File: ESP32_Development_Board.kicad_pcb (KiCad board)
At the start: 2 copper layers, 47 parts, among them J1 Conn_01x17_Pin, J2 Conn_01x17_Pin, J3 Conn_01x03_Pin, J4 USB_B_Micro, J5 Conn_01x02_Pin, Q1 NPN, Q2 NPN, Q3 Q_NMOS_GDS, Q4 Q_NMOS_GDS, SW1 SW_Push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

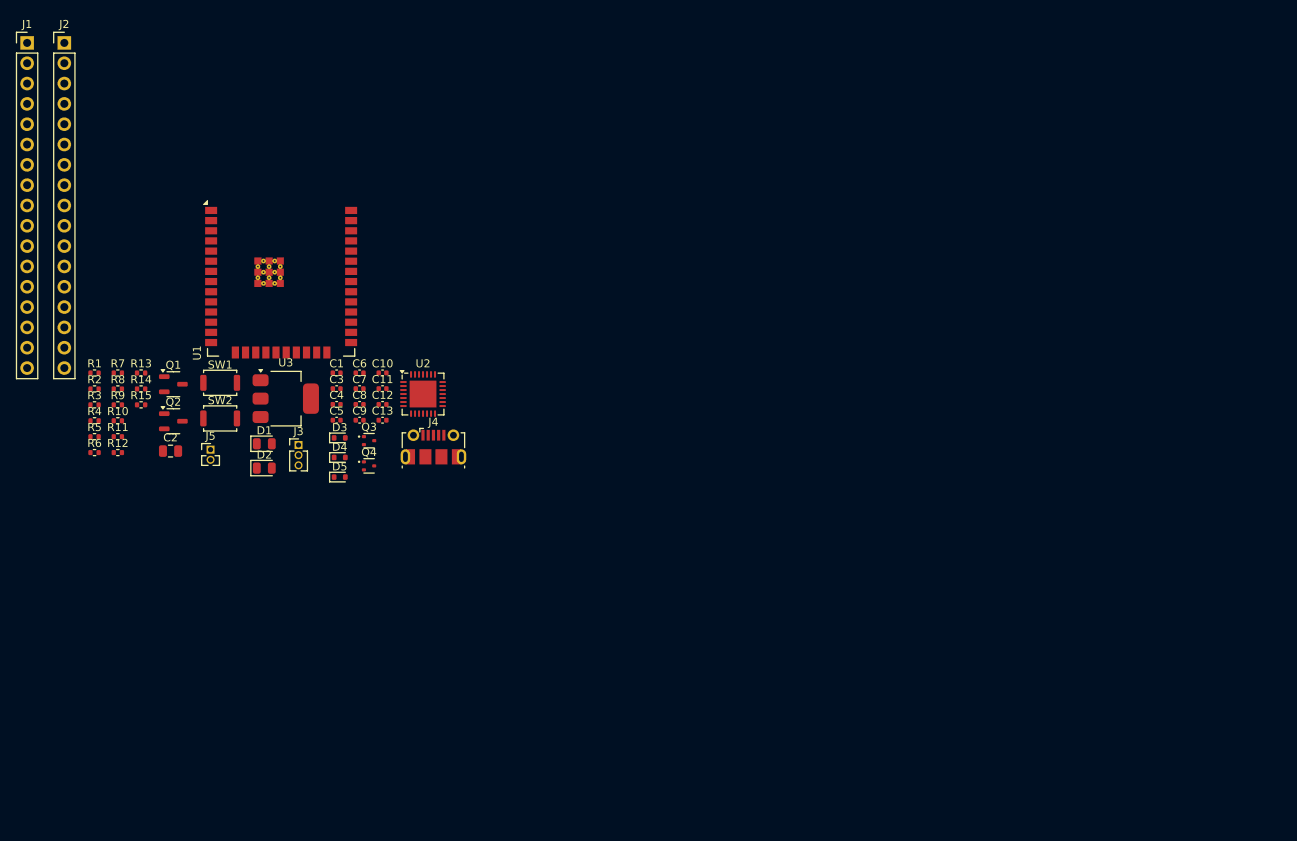
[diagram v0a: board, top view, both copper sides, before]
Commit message: Placed Components
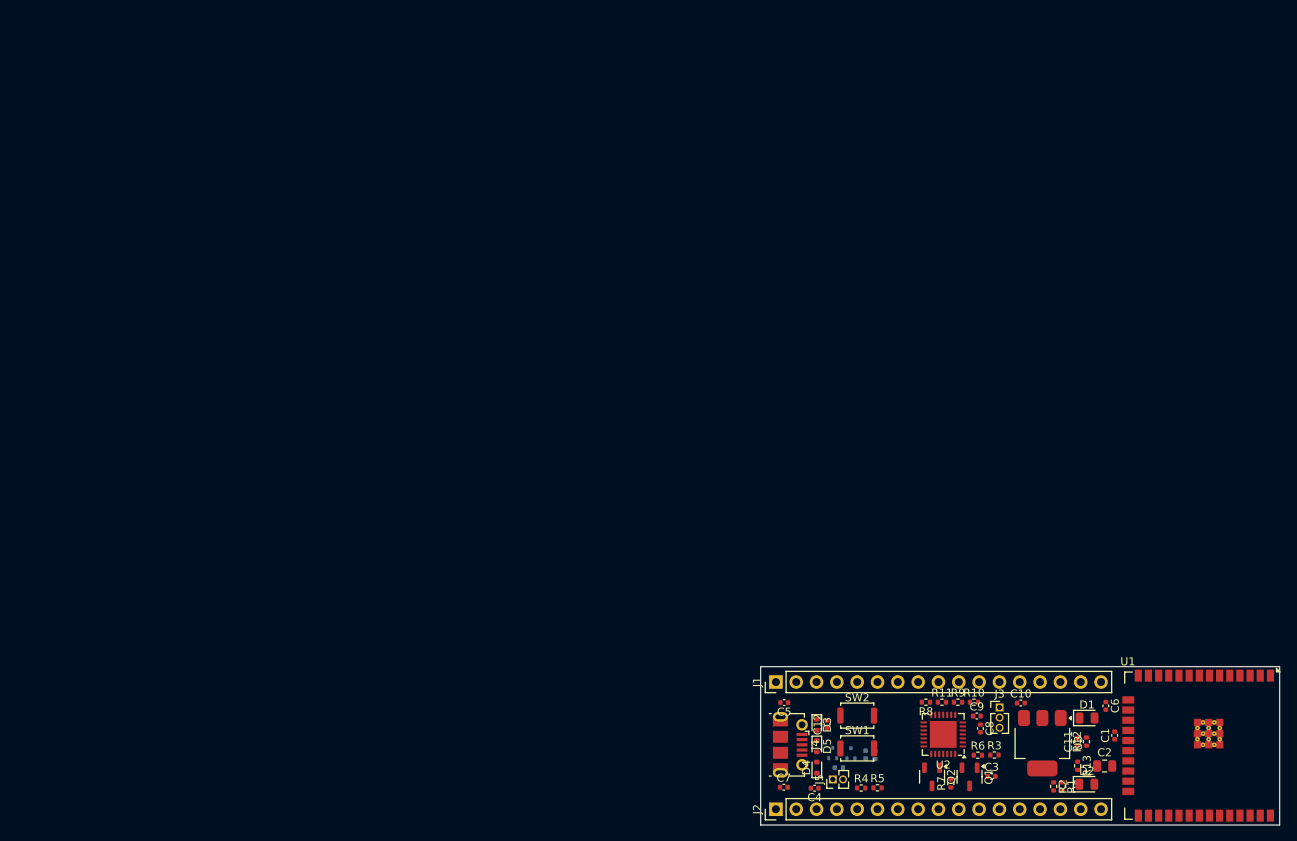
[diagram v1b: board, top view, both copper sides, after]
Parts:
- C13, Q3, Q4, R14, R15: moved to B.Cu
- moved U1 133.5 mm to (191.4, 102.6), turned to -90 degrees
- moved R1 131.5 mm to (170.6, 107.7), turned to -90 degrees
- moved J2 130.7 mm to (134.8, 110.5), turned to 90 degrees
- moved R2 129.8 mm to (169.5, 107.7), turned to -90 degrees
- moved R13 126.9 mm to (172.5, 105.1), turned to -90 degrees
- moved R12 126.4 mm to (173.6, 102.1), turned to 90 degrees
- moved C2 123.2 mm to (175.9, 105.2)
- moved J1 123.1 mm to (134.8, 94.7), turned to 90 degrees
- moved R3 120.7 mm to (162.1, 103.8)
- moved R6 116.7 mm to (160.1, 103.8)
- moved R7 116.1 mm to (156.7, 107.3), turned to 90 degrees
- moved R10 112.6 mm to (159.6, 97.2)
- moved R9 111.4 mm to (157.6, 97.2)
- moved Q1 111.0 mm to (159.0, 106.5), turned to -90 degrees
- moved D2 110.1 mm to (173.7, 107.4)
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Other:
- board outline added: 64.9 x 19.8 mm

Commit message: Aug 16, 2025
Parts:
- J5: moved to B.Cu
- U3: footprint Package_TO_SOT_SMD:SOT-223-3_TabPin2 -> Package_TO_SOT_SMD:SOT-89-3
- moved R1 97.4 mm to (76.0, 84.4), turned to 0 degrees
- moved R2 95.9 mm to (76.0, 86.4), turned to 0 degrees
- moved R13 93.1 mm to (81.8, 84.4), turned to 0 degrees
- moved C2 91.1 mm to (85.5, 94.2)
- moved C1 87.8 mm to (90.3, 88.6), turned to 0 degrees
- moved D2 85.7 mm to (91.1, 84.5)
- moved R6 84.6 mm to (76.0, 94.4)
- moved R7 81.1 mm to (78.9, 84.4), turned to 0 degrees
- moved R10 81.0 mm to (78.9, 90.4)
- moved R9 79.2 mm to (78.9, 88.4)
- moved R11 76.8 mm to (78.9, 92.4)
- moved Q1 76.0 mm to (85.8, 85.8), turned to 0 degrees
- moved R8 75.4 mm to (78.9, 86.4), turned to 0 degrees
- moved R5 73.2 mm to (76.0, 92.4)
- moved R4 71.7 mm to (76.0, 90.4)
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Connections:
- D4 pad 2: /USB_DN -> /USB_DP
- D5 pad 2: /USB_DP -> /USB_DN
- J4 pad 2: /USB_DP -> /USB_DN
- J4 pad 3: /USB_DN -> /USB_DP
- Q3 pad 2: /USB_DN -> /USB_DP
- Q4 pad 2: /USB_DP -> /USB_DN
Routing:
- net GND: track 0.00 -> 25.7 mm, vias 0 -> 14
- net +3.3V: track 0.00 -> 22.4 mm, vias 0 -> 4
- net Net-(J5-Pin_2): track 0.00 -> 10.9 mm
- net +5VD: track 0.00 -> 6.58 mm
- net /EN: track 0.00 -> 5.38 mm
- net /USB_DN: track 0.00 -> 5.13 mm, vias 0 -> 1
- net /USB_DP: track 0.00 -> 5.12 mm, vias 0 -> 1
- net +5VA: track 0.00 -> 4.89 mm
- net +5V: track 0.00 -> 4.10 mm
- net /IO23: track 0.00 -> 3.79 mm
- net Net-(D1-A): track 0.00 -> 1.68 mm
- added copper zone on In1.Cu, net +3.3V
- added copper zone on In2.Cu, net GND
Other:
- board size 64.9 x 19.8 mm -> 70 x 20.3 mm
- copper layers 2 -> 4

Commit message: Commit at 2025-08-18 15:00:00
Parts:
- moved R2 83.6 mm to (157.6, 104.8), turned to -90 degrees
- moved R1 74.9 mm to (148.8, 101.8), turned to 180 degrees
- moved C2 70.9 mm to (156.3, 91.8), turned to 90 degrees
- moved C1 67.1 mm to (157.1, 94.7), turned to -90 degrees
- moved R5 63.1 mm to (138.5, 100.6), turned to 90 degrees
- moved R4 62.3 mm to (137.4, 100.6), turned to 90 degrees
- moved R9 61.5 mm to (140.2, 92.3), turned to -90 degrees
- moved R10 60.3 mm to (139.2, 92.3), turned to 90 degrees
- moved R11 59.2 mm to (138.1, 92.3), turned to -90 degrees
- moved R8 58.4 mm to (137.0, 92.3), turned to 90 degrees
- moved C8 49.0 mm to (142.1, 94.6), turned to 90 degrees
- moved C9 47.9 mm to (141.0, 94.6), turned to 90 degrees
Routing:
- net GND: track 25.7 -> 31.3 mm, vias 14 -> 16
- net Net-(U1-IO0): track 0.00 -> 3.27 mm
- net +3.3V: track 22.4 -> 25.5 mm, vias 4 -> 5
- net /IO0_CON: track 0.00 -> 2.43 mm

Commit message: Commit at 2025-08-18 17:00:00
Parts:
- moved R6 66.4 mm to (142.1, 100.6), turned to -90 degrees
- moved R7 60.6 mm to (137.1, 101.1), turned to -90 degrees
- moved Q2 60.1 mm to (145.1, 100.5), turned to 180 degrees
- moved R13 53.5 mm to (133.9, 96.2), turned to 90 degrees
- moved Q1 50.8 mm to (134.5, 100.5)
- moved D2 46.1 mm to (135.5, 96.9), turned to 90 degrees
- moved C4 34.6 mm to (124.7, 95.5)
- moved U2 2.48 mm to (139.8, 96.5)
- moved C8 2.47 mm to (144.6, 94.6)
- moved C9 2.47 mm to (143.5, 94.6)
- moved R10 2.47 mm to (141.7, 92.3)
- moved R11 2.47 mm to (140.6, 92.3)
- moved R4 2.47 mm to (139.9, 100.6)
- moved R5 2.47 mm to (141.0, 100.6)
- moved R8 2.47 mm to (139.5, 92.3)
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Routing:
- net GND: track 31.3 -> 37.7 mm, vias 16 -> 20
- net +3.3V: track 25.5 -> 31.4 mm, vias 5 -> 7
- net /DTR: track 0.00 -> 3.59 mm
- net /USB_DN: track 5.13 -> 8.14 mm, vias 1 -> 2
- net /USB_DP: track 5.12 -> 8.13 mm, vias 1 -> 2
- net Net-(U2-VBUS): track 0.00 -> 2.42 mm
- net /TXD: track 0.00 -> 1.44 mm
- net Net-(U2-~{SUSPEND}): track 0.00 -> 1.34 mm
- net Net-(U2-~{RST}): track 0.00 -> 1.32 mm
- net /RXD: track 0.00 -> 1.22 mm
- net +5VA: track 4.89 -> 5.88 mm, vias 0 -> 1

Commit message: Commit at 2025-08-18 18:00:00
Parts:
- moved R7 1.77 mm to (138.8, 100.6)
- moved R15 1.40 mm to (118.3, 101.8)
- moved R14 1.01 mm to (118.3, 99.7), turned to 180 degrees
- moved C13 0.98 mm to (118.3, 100.7), turned to 180 degrees
- moved Q3 0.92 mm to (118.5, 97.9)
- moved Q4 0.89 mm to (118.3, 93.8)
- moved C6 0.41 mm to (155.8, 87.8)
- moved C8 0.36 mm to (144.6, 94.3)
- moved C9 0.36 mm to (143.5, 94.3)
- moved Q1 0.09 mm to (134.5, 100.5)
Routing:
- net /USB_DP: track 8.13 -> 33.8 mm
- net /USB_DN: track 8.14 -> 33.8 mm
- net Net-(J5-Pin_2): track 10.9 -> 0.01 mm
- net GND: track 37.7 -> 27.6 mm, vias 20 -> 17
- net +3.3V: track 31.4 -> 24.9 mm, vias 7 -> 9
- net /RTS: track 0.00 -> 4.72 mm
- net Net-(D2-A): track 0.00 -> 1.70 mm
- net /IO23: track 3.79 -> 2.39 mm

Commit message: Commit at 2025-08-18 20:04:58
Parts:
- moved J5 1.43 mm to (120.9, 99.8)
- moved Q3 0.58 mm to (118.5, 97.4)
- moved Q4 0.47 mm to (118.4, 94.3)
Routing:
- net Net-(J5-Pin_2): track 0.01 -> 19.4 mm
- net GND: track 27.6 -> 32.3 mm, vias 17 -> 19
- net /USB_DP: track 33.8 -> 35.0 mm
- net /USB_DN: track 33.8 -> 35.0 mm
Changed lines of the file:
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@@
 	(footprint "Connector_PinHeader_1.27mm:PinHeader_1x02_P1.27mm_Vertical"
 		(layer "B.Cu")
-		(at 121.825 98.7 180)
+		(at 120.94 99.82 180)
 		(descr "Through hole straight pin header, 1x02, 1.27mm pitch, single row")
 		(tags "Through hole pin header THT 1x02 1.27mm single row")
@@
 	(footprint "Package_TO_SOT_SMD:SOT-523"
 		(layer "B.Cu")
-		(at 118.45 97.94)
+		(at 118.455 97.36)
 		(descr "SOT523, https://www.diodes.com/assets/Package-Files/SOT523.pdf")
 		(tags "SOT-523")
@@
 	(footprint "Package_TO_SOT_SMD:SOT-523"
 		(layer "B.Cu")
-		(at 118.35 93.8175 90)
+		(at 118.36 94.29 90)
 		(descr "SOT523, https://www.diodes.com/assets/Package-Files/SOT523.pdf")
 		(tags "SOT-523")
@@
 	)
 	(via
+		(at 116.9 99.66)
+		(size 0.6)
+		(drill 0.3)
+		(layers "F.Cu" "B.Cu")
+		(net 1)
+	)
+	(via
 		(at 156.65 87.37)
 		(size 0.6)
@@
 	)
 	(via
+		(at 118.83 98.35)
+		(size 0.6)
+		(drill 0.3)
+		(layers "F.Cu" "B.Cu")
+		(net 1)
+	)
+	(via
 		(at 116.225 90.825)
 		(size 0.6)
 		(drill 0.3)
 		(layers "F.Cu" "B.Cu")
+		(net 1)
+	)
+	(segment
+		(start 117.81 100.67)
+		(end 117.87 100.73)
+		(width 0.5334)
+		(layer "B.Cu")
+		(net 1)
+	)
+	(segment
+		(start 116.9 93.95)
+		(end 117.205 93.645)
+		(width 0.5334)
+		(layer "B.Cu")
+		(net 1)
+	)
+	(segment
+		(start 117.205 93.645)
+		(end 118.36 93.645)
+		(width 0.5334)
+		(layer "B.Cu")
+		(net 1)
+	)
+	(segment
+		(start 119.1 97.36)
+		(end 119.1 98.08)
+		(width 0.5334)
+		(layer "B.Cu")
+		(net 1)
+	)
+	(segment
+		(start 117.81 99.66)
+		(end 117.81 100.67)
+		(width 0.5334)
+		(layer "B.Cu")
+		(net 1)
+	)
+	(segment
+		(start 119.1 98.08)
+		(end 118.83 98.35)
+		(width 0.5334)
+		(layer "B.Cu")
+		(net 1)
+	)
+	(segment
+		(start 117.81 99.66)
+		(end 116.9 99.66)
+		(width 0.5334)
+		(layer "B.Cu")
 		(net 1)
 	)
@@
 	)
 	(segment
-		(start 118.83 101.8)
+		(start 118.83 99.66)
+		(end 118.83 99.3)
+		(width 0.2)
+		(layer "B.Cu")
+		(net 8)
+	)
+	(segment
+		(start 116.3 98.32)
+		(end 116.69 98.71)
+		(width 0.2)
+		(layer "B.Cu")
+		(net 8)
+	)
+	(segment
+		(start 117.81 98.28)
+		(end 117.81 97.86)
+		(width 0.2)
+		(layer "B.Cu")
+		(net 8)
+	)
+	(segment
+		(start 116.7 92.72)
+		(end 116.3 93.12)
+		(width 0.2)
+		(layer "B.Cu")
+		(net 8)
+	)
+	(segment
+		(start 116.69 98.71)
+		(end 117.38 98.71)
+		(width 0.2)
+		(layer "B.Cu")
+		(net 8)
+	)
+	(segment
+		(start 119.18 92.72)
+		(end 116.7 92.72)
+		(width 0.2)
+		(layer "B.Cu")
+		(net 8)
+	)
+	(segment
+		(start 116.3 93.12)
+		(end 116.3 98.32)
+		(width 0.2)
+		(layer "B.Cu")
+		(net 8)
+	)
+	(segment
+		(start 120.54 101.09)
+		(end 119.82 101.81)
+		(width 0.2)
+		(layer "B.Cu")
+		(net 8)
+	)
+	(segment
+		(start 119.82 101.81)
 		(end 118.83 101.81)
+		(width 0.2)
+		(layer "B.Cu")
+		(net 8)
+	)
+	(segment
+		(start 118.86 94.935)
+		(end 118.86 94.42)
+		(width 0.2)
+		(layer "B.Cu")
+		(net 8)
+	)
+	(segment
+		(start 117.38 98.71)
+		(end 117.81 98.28)
+		(width 0.2)
+		(layer "B.Cu")
+		(net 8)
+	)
+	(segment
+		(start 119.4 93.88)
+		(end 119.4 92.94)
+		(width 0.2)
+		(layer "B.Cu")
+		(net 8)
+	)
+	(segment
+		(start 119.4 92.94)
+		(end 119.18 92.72)
+		(width 0.2)
+		(layer "B.Cu")
+		(net 8)
+	)
+	(segment
+		(start 118.83 99.66)
+		(end 118.83 101.81)
+		(width 0.2)
+		(layer "B.Cu")
+		(net 8)
+	)
+	(segment
+		(start 120.94 101.09)
+		(end 120.54 101.09)
+		(width 0.2)
+		(layer "B.Cu")
+		(net 8)
+	)
+	(segment
+		(start 118.83 99.3)
+		(end 117.81 98.28)
+		(width 0.2)
+		(layer "B.Cu")
+		(net 8)
+	)
+	(segment
+		(start 118.86 94.42)
+		(end 119.4 93.88)
 		(width 0.2)
 		(layer "B.Cu")
@@
 	)
 	(segment
+		(start 117.315 94.935)
+		(end 116.9 95.35)
+		(width 0.2)
+		(layer "B.Cu")
+		(net 12)
+	)
+	(segment
 		(start 119.469301 95.712499)
 		(end 120.0468 95.135)
@@
 	)
 	(segment
+		(start 117.86 94.935)
+		(end 117.315 94.935)
+		(width 0.2)
+		(layer "B.Cu")
+		(net 12)
+	)
+	(segment
 		(start 143.530001 96.400001)
 		(end 143.8925 96.7625)
@@
 	)
 	(segment
+		(start 117.81 96.86)
+		(end 117.09 96.86)
+		(width 0.2)
+		(layer "B.Cu")
+		(net 13)
+	)
+	(segment
+		(start 117.09 96.86)
+		(end 116.9 96.67)
+		(width 0.2)
+		(layer "B.Cu")
+		(net 13)
+	)
+	(segment
 		(start 116.9 96.525)
 		(end 117.262499 96.162501)
@@
 		(width 0.2)
 		(layer "B.Cu")
+		(net 13)
+	)
+	(segment
+		(start 116.9 96.67)
+		(end 116.9 96.525)
+		(width 0.2)
+		(layer "B.Cu")

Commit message: Commit at 2025-08-20 15:00:01
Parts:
- moved SW2 5.62 mm to (124.7, 93.0), turned to -90 degrees
- moved C4 4.83 mm to (122.4, 91.2), turned to -90 degrees
- moved C3 3.16 mm to (121.3, 93.2)
- moved R3 3.16 mm to (121.3, 91.2)
- moved SW1 0.54 mm to (119.0, 93.0), turned to -90 degrees
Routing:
- net GND: track 32.3 -> 41.9 mm, vias 19 -> 21
- net /IO0_BTN: track 0.00 -> 2.40 mm
- net /EN: track 5.38 -> 7.43 mm

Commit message: Commit at 2025-08-20 16:00:00
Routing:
- net /EN: track 7.43 -> 68.7 mm, vias 0 -> 1
- net /I39: track 0.00 -> 60.6 mm, vias 0 -> 1
- net /I36: track 0.00 -> 56.8 mm, vias 0 -> 1
- net /I34: track 0.00 -> 55.1 mm, vias 0 -> 1
- net /I35: track 0.00 -> 51.3 mm, vias 0 -> 1
- net /IO32: track 0.00 -> 46.3 mm, vias 0 -> 1
- net /IO33: track 0.00 -> 42.1 mm, vias 0 -> 1
- net /IO25: track 0.00 -> 38.0 mm, vias 0 -> 1
- net /IO26: track 0.00 -> 34.2 mm, vias 0 -> 1
- net /IO27: track 0.00 -> 28.7 mm, vias 0 -> 1
- net /IO14: track 0.00 -> 23.7 mm, vias 0 -> 1
- net /IO12: track 0.00 -> 19.6 mm, vias 0 -> 1
- net GND: track 41.9 -> 46.2 mm, vias 21 -> 23
- net /IO23: track 2.39 -> 4.25 mm, vias 0 -> 1
- net /TXD0: track 0.00 -> 1.86 mm, vias 0 -> 1
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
